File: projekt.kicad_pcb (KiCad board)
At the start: 2 copper layers, 75 x 35 mm, 32 parts, among them J1 Conn_Coaxial, J2 OLED, SW1 SW_DIP_x01, U1 AD8307, U2 L7805

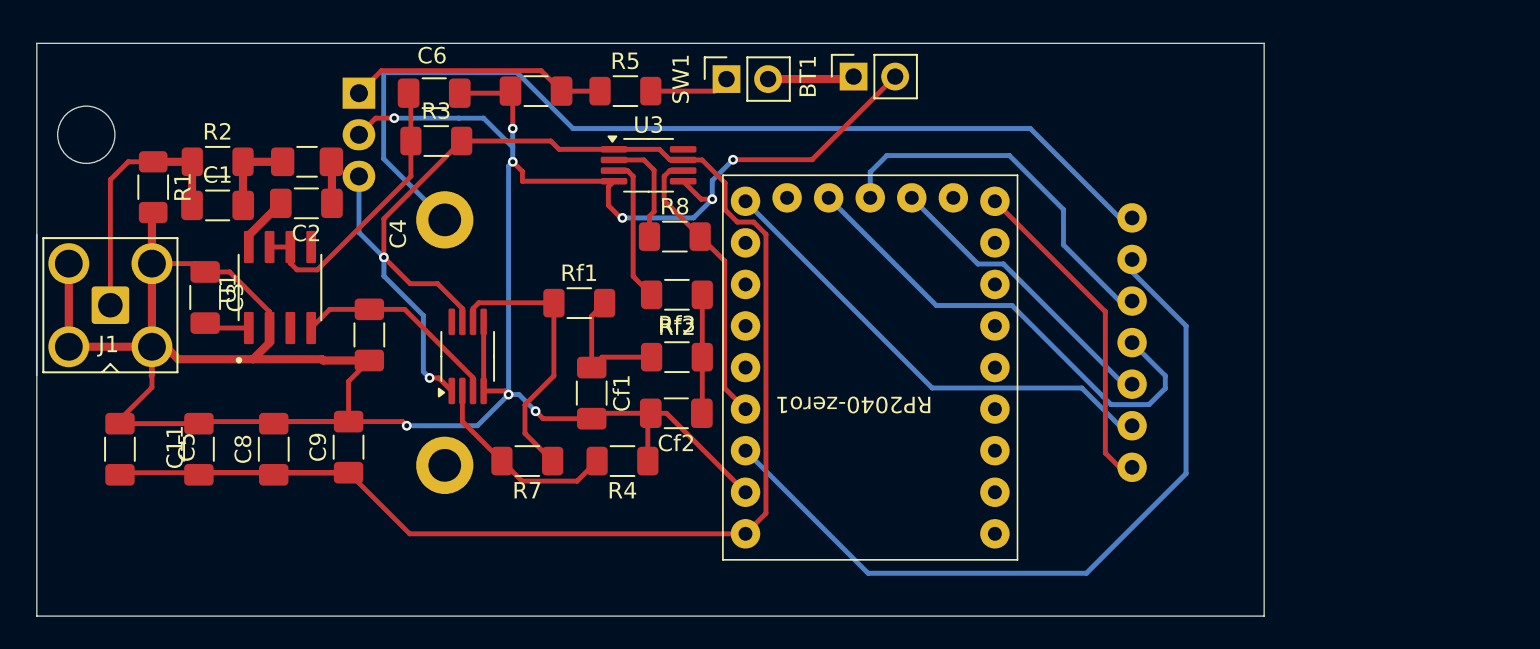
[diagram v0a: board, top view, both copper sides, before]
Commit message: dodane C10
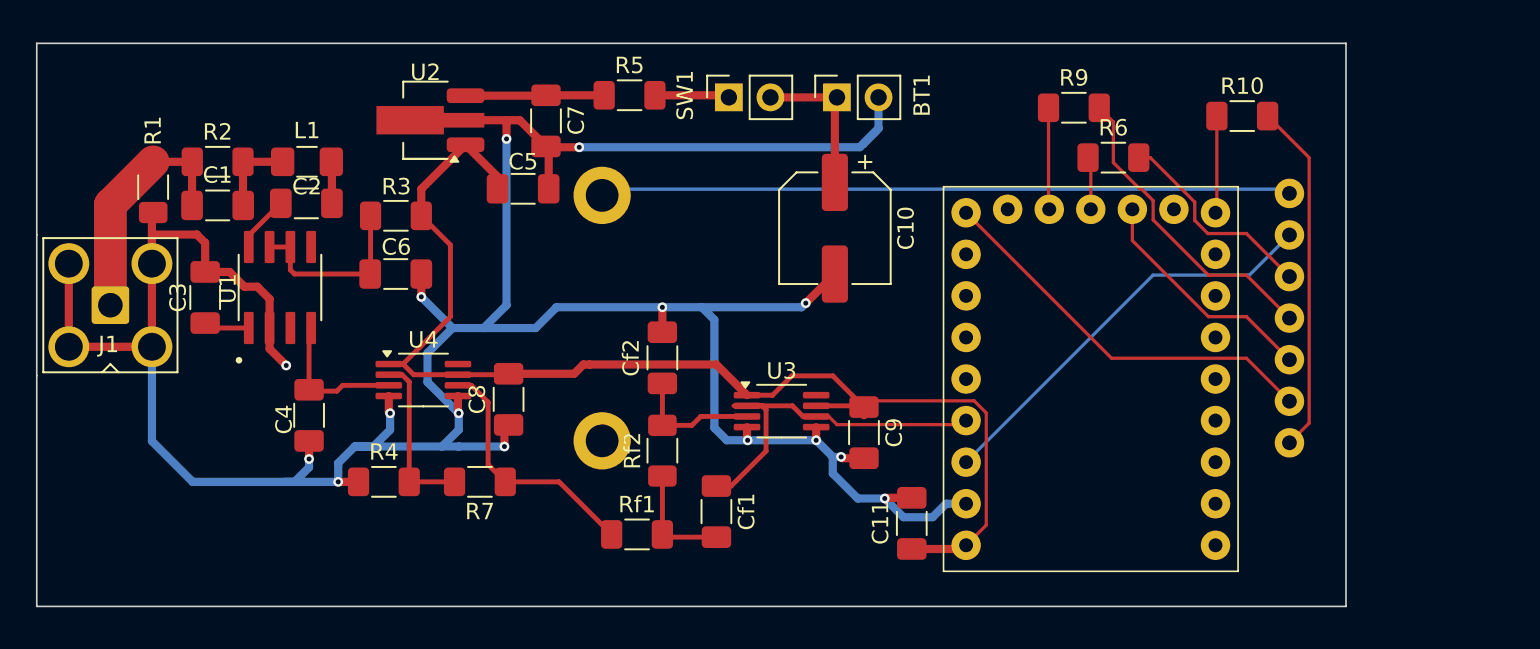
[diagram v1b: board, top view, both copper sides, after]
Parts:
- removed R8: 1k, Resistor_SMD:R_1206_3216Metric_Pad1.30x1.75mm_HandSolder
- removed Rf3: 10k, Resistor_SMD:R_1206_3216Metric_Pad1.30x1.75mm_HandSolder
- added C10: 10u, Capacitor_SMD:CP_Elec_6.3x5.3, F.Cu at (61.5, 33.4)
- added R10: 10, Resistor_SMD:R_1206_3216Metric_Pad1.30x1.75mm_HandSolder, F.Cu at (86.4, 26.5)
- added R6: 10, Resistor_SMD:R_1206_3216Metric_Pad1.30x1.75mm_HandSolder, F.Cu at (78.5, 29.1)
- added R9: 10, Resistor_SMD:R_1206_3216Metric_Pad1.30x1.75mm_HandSolder, F.Cu at (76.1, 26.0)
- U2: footprint Package_TO_SOT_THT:TO-220-3_Horizontal_TabDown -> Package_TO_SOT_SMD:SOT-89-3_Handsoldering; moved to F.Cu
- moved C11 48.6 mm to (66.2, 51.4)
- moved C9 31.5 mm to (63.2, 45.9), turned to -90 degrees
- moved C5 25.4 mm to (42.4, 31.0), turned to 0 degrees
- moved U3 17.1 mm to (58.2, 44.6)
- moved C8 14.7 mm to (41.5, 43.9), turned to -90 degrees
- moved R4 14.6 mm to (33.9, 48.9), turned to 0 degrees
- moved Rf1 14.6 mm to (49.4, 52.1)
- moved RP2040-zero1 13.5 mm to (86.1, 30.9)
- moved C6 11.3 mm to (34.6, 36.2)
- moved Cf1 10.5 mm to (54.2, 50.7)
- moved J2 9.73 mm to (90.7, 48.9)
- moved C4 6.14 mm to (29.3, 44.8)
- moved Rf2 5.78 mm to (50.9, 47.0), turned to 90 degrees
- moved R3 5.19 mm to (34.6, 32.6)
- moved U2 4.39 mm to (36.4, 26.8), turned to 180 degrees
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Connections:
- Cf1 pad 1: Net-(Cf1-Pad1) -> /RF/RF_OUT
- Cf1 pad 2: GNDPWR -> Net-(Cf1-Pad2)
- Cf2 pad 1: Net-(Cf2-Pad1) -> Net-(U3-+)
- RP2040-zero1 pad 10: /uC/CS -> Net-(RP2040-zero1-GP13)
- RP2040-zero1 pad 12: /uC/SDA -> Net-(RP2040-zero1-GP11)
- RP2040-zero1 pad 13: /uC/SCK -> Net-(RP2040-zero1-GP10)
- Rf1 pad 2: Net-(Cf1-Pad1) -> Net-(Cf1-Pad2)
- Rf2 pad 1: Net-(Cf1-Pad1) -> Net-(Cf1-Pad2)
- Rf2 pad 2: Net-(Cf2-Pad1) -> Net-(U3-+)
- U2 pad 1: Net-(U2-IN) -> VCC
- U2 pad 3: VCC -> Net-(U2-IN)
- U3 pad 2: Net-(U3--) -> /RF/RF_OUT
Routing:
- net VCC: track 126.5 -> 75.0 mm, vias 2 -> 0
- net /uC/3V3: track 46.8 -> 25.5 mm
- net /uC/GND: track 59.7 -> 42.3 mm
- net GNDPWR: track 178.7 -> 194.9 mm, vias 9 -> 15
- net /uC/SDA: track 29.9 -> 19.1 mm
- net /uC/SCK: track 22.7 -> 12.9 mm
- net Net-(Cf1-Pad1): track 8.18 -> 0.00 mm
- net Net-(Cf2-Pad1): track 7.50 -> 0.00 mm
- net Net-(U2-IN): track 15.9 -> 8.52 mm
- net Net-(Cf1-Pad2): track 0.00 -> 7.00 mm
- net Net-(U3--): track 6.88 -> 0.00 mm
- net Net-(RP2040-zero1-GP11): track 0.00 -> 6.22 mm
- net Net-(U1-ENB): track 17.3 -> 11.2 mm
- net Net-(RP2040-zero1-GP13): track 0.00 -> 5.94 mm
- net /RF/RF_OUT: track 17.6 -> 22.5 mm
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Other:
- board size 75 x 35 mm -> 80 x 34.4 mm

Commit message: test111
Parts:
- removed C10: 10u, Capacitor_SMD:CP_Elec_6.3x5.3
- added C12: 100n, Capacitor_SMD:C_1206_3216Metric_Pad1.33x1.80mm_HandSolder, F.Cu at (66.3, 51.5)
- C11: value 100n -> 10u; footprint Capacitor_SMD:C_1206_3216Metric_Pad1.33x1.80mm_HandSolder -> Capacitor_SMD:CP_Elec_6.3x5.3
- moved C11 16.8 mm to (63.8, 34.8)
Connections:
- C11 pad 1: GNDPWR -> VCC
- C11 pad 2: VCC -> GNDPWR
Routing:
- net GNDPWR: track 194.9 -> 192.2 mm, vias 15 -> 14

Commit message: test2
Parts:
- added C10: 10n, Capacitor_SMD:C_1206_3216Metric_Pad1.33x1.80mm_HandSolder, F.Cu at (99.8, 25.1)
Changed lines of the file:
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@@
+	)
+	(footprint "Capacitor_SMD:C_1206_3216Metric_Pad1.33x1.80mm_HandSolder"
+		(layer "F.Cu")
+		(at 99.7835 25.146)
+		(descr "Capacitor SMD 1206 (3216 Metric), square (rectangular) end terminal, IPC_7351 nominal with elongated pad for handsoldering. (Body size source: IPC-SM-782 page 76, https://www.pcb-3d.com/wordpress/wp-content/uploads/ipc-sm-782a_amendment_1_and_2.pdf), generated with kicad-footprint-generator")
+		(tags "capacitor handsolder")
+		(property "Reference" "C10"
+			(at 0 -1.85 0)
+			(layer "F.SilkS")
+			(effects
+				(font
+					(size 1 1)
+					(thickness 0.15)
+				)
+			)
+		)
+		(property "Value" "10n"
+			(at 0 1.85 0)
+			(layer "F.Fab")
+			(effects
+				(font
+					(size 1 1)
+					(thickness 0.15)
+				)
+			)
+		)
+		(property "Footprint" "Capacitor_SMD:C_1206_3216Metric_Pad1.33x1.80mm_HandSolder"
+			(at 0 0 0)
+			(unlocked yes)
+			(layer "F.Fab")
+			(hide yes)
+			(effects
+				(font
+					(size 1.27 1.27)
+					(thickness 0.15)
+				)
+			)
+		)
+		(property "Datasheet" ""
+			(at 0 0 0)
+			(unlocked yes)
+			(layer "F.Fab")
+			(hide yes)
+			(effects
+				(font
+					(size 1.27 1.27)
+					(thickness 0.15)
+				)
+			)
+		)
+		(property "Description" "Unpolarized capacitor"
+			(at 0 0 0)
+			(unlocked yes)
+			(layer "F.Fab")
+			(hide yes)
+			(effects
+				(font
+					(size 1.27 1.27)
+					(thickness 0.15)
+				)
+			)
+		)
+		(property ki_fp_filters "C_*")
+		(sheetname "uC")
+		(sheetfile "uC.kicad_sch")
+		(attr smd)
+		(fp_line
+			(start -0.711252 -0.91)
+			(end 0.711252 -0.91)
+			(stroke
+				(width 0.12)
+				(type solid)
+			)
+			(layer "F.SilkS")
+		)
+		(fp_line
+			(start -0.711252 0.91)
+			(end 0.711252 0.91)
+			(stroke
+				(width 0.12)
+				(type solid)
+			)
+			(layer "F.SilkS")
+		)
+		(fp_line
+			(start -2.48 -1.15)
+			(end 2.48 -1.15)
+			(stroke
+				(width 0.05)
+				(type solid)
+			)
+			(layer "F.CrtYd")
+		)
+		(fp_line
+			(start -2.48 1.15)
+			(end -2.48 -1.15)
+			(stroke
+				(width 0.05)
+				(type solid)
+			)
+			(layer "F.CrtYd")
+		)
+		(fp_line
+			(start 2.48 -1.15)
+			(end 2.48 1.15)
+			(stroke
+				(width 0.05)
+				(type solid)
+			)
+			(layer "F.CrtYd")
+		)
+		(fp_line
+			(start 2.48 1.15)
+			(end -2.48 1.15)
+			(stroke
+				(width 0.05)
+				(type solid)
+			)
+			(layer "F.CrtYd")
+		)
+		(fp_line
+			(start -1.6 -0.8)
+			(end 1.6 -0.8)
+			(stroke
+				(width 0.1)
+				(type solid)
+			)
+			(layer "F.Fab")
+		)
+		(fp_line
+			(start -1.6 0.8)
+			(end -1.6 -0.8)
+			(stroke
+				(width 0.1)
+				(type solid)
+			)
+			(layer "F.Fab")
+		)
+		(fp_line
+			(start 1.6 -0.8)
+			(end 1.6 0.8)
+			(stroke
+				(width 0.1)
+				(type solid)
+			)
+			(layer "F.Fab")
+		)
+		(fp_line
+			(start 1.6 0.8)
+			(end -1.6 0.8)
+			(stroke
+				(width 0.1)
+				(type solid)
+			)
+			(layer "F.Fab")
+		)
+		(fp_text user "${REFERENCE}"
+			(at 0 0 0)
+			(layer "F.Fab")
+			(effects
+				(font
+					(size 0.8 0.8)
+					(thickness 0.12)
+				)
+			)
+		)
+		(pad "1" smd roundrect
+			(at -1.5625 0)
+			(size 1.325 1.8)
+			(layers "F.Cu" "F.Paste" "F.Mask")
+			(roundrect_rratio 0.188679)
+			(net 5 "VCC")
+			(pintype "passive")
+		)
+		(pad "2" smd roundrect
+			(at 1.5625 0)
+			(size 1.325 1.8)
+			(layers "F.Cu" "F.Paste" "F.Mask")
+			(roundrect_rratio 0.188679)
+			(net 1 "GNDPWR")
+			(pintype "passive")
+		)
+		(model "${KICAD8_3DMODEL_DIR}/Capacitor_SMD.3dshapes/C_1206_3216Metric.wrl"
+			(offset
+				(xyz 0 0 0)
+			)
+			(scale
+				(xyz 1 1 1)
+			)
+			(rotate
+				(xyz 0 0 0)
+			)
+		)
 	)
 	(footprint "Capacitor_SMD:C_1206_3216Metric_Pad1.33x1.80mm_HandSolder"

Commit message: Kondensator usunięty Test2
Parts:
- removed C10: 10n, Capacitor_SMD:C_1206_3216Metric_Pad1.33x1.80mm_HandSolder
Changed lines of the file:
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@@
-	)
-	(footprint "Capacitor_SMD:C_1206_3216Metric_Pad1.33x1.80mm_HandSolder"
-		(layer "F.Cu")
-		(at 99.7835 25.146)
-		(descr "Capacitor SMD 1206 (3216 Metric), square (rectangular) end terminal, IPC_7351 nominal with elongated pad for handsoldering. (Body size source: IPC-SM-782 page 76, https://www.pcb-3d.com/wordpress/wp-content/uploads/ipc-sm-782a_amendment_1_and_2.pdf), generated with kicad-footprint-generator")
-		(tags "capacitor handsolder")
-		(property "Reference" "C10"
-			(at 0 -1.85 0)
-			(layer "F.SilkS")
-			(effects
-				(font
-					(size 1 1)
-					(thickness 0.15)
-				)
-			)
-		)
-		(property "Value" "10n"
-			(at 0 1.85 0)
-			(layer "F.Fab")
-			(effects
-				(font
-					(size 1 1)
-					(thickness 0.15)
-				)
-			)
-		)
-		(property "Footprint" "Capacitor_SMD:C_1206_3216Metric_Pad1.33x1.80mm_HandSolder"
-			(at 0 0 0)
-			(unlocked yes)
-			(layer "F.Fab")
-			(hide yes)
-			(effects
-				(font
-					(size 1.27 1.27)
-					(thickness 0.15)
-				)
-			)
-		)
-		(property "Datasheet" ""
-			(at 0 0 0)
-			(unlocked yes)
-			(layer "F.Fab")
-			(hide yes)
-			(effects
-				(font
-					(size 1.27 1.27)
-					(thickness 0.15)
-				)
-			)
-		)
-		(property "Description" "Unpolarized capacitor"
-			(at 0 0 0)
-			(unlocked yes)
-			(layer "F.Fab")
-			(hide yes)
-			(effects
-				(font
-					(size 1.27 1.27)
-					(thickness 0.15)
-				)
-			)
-		)
-		(property ki_fp_filters "C_*")
-		(sheetname "uC")
-		(sheetfile "uC.kicad_sch")
-		(attr smd)
-		(fp_line
-			(start -0.711252 -0.91)
-			(end 0.711252 -0.91)
-			(stroke
-				(width 0.12)
-				(type solid)
-			)
-			(layer "F.SilkS")
-		)
-		(fp_line
-			(start -0.711252 0.91)
-			(end 0.711252 0.91)
-			(stroke
-				(width 0.12)
-				(type solid)
-			)
-			(layer "F.SilkS")
-		)
-		(fp_line
-			(start -2.48 -1.15)
-			(end 2.48 -1.15)
-			(stroke
-				(width 0.05)
-				(type solid)
-			)
-			(layer "F.CrtYd")
-		)
-		(fp_line
-			(start -2.48 1.15)
-			(end -2.48 -1.15)
-			(stroke
-				(width 0.05)
-				(type solid)
-			)
-			(layer "F.CrtYd")
-		)
-		(fp_line
-			(start 2.48 -1.15)
-			(end 2.48 1.15)
-			(stroke
-				(width 0.05)
-				(type solid)
-			)
-			(layer "F.CrtYd")
-		)
-		(fp_line
-			(start 2.48 1.15)
-			(end -2.48 1.15)
-			(stroke
-				(width 0.05)
-				(type solid)
-			)
-			(layer "F.CrtYd")
-		)
-		(fp_line
-			(start -1.6 -0.8)
-			(end 1.6 -0.8)
-			(stroke
-				(width 0.1)
-				(type solid)
-			)
-			(layer "F.Fab")
-		)
-		(fp_line
-			(start -1.6 0.8)
-			(end -1.6 -0.8)
-			(stroke
-				(width 0.1)
-				(type solid)
-			)
-			(layer "F.Fab")
-		)
-		(fp_line
-			(start 1.6 -0.8)
-			(end 1.6 0.8)
-			(stroke
-				(width 0.1)
-				(type solid)
-			)
-			(layer "F.Fab")
-		)
-		(fp_line
-			(start 1.6 0.8)
-			(end -1.6 0.8)
-			(stroke
-				(width 0.1)
-				(type solid)
-			)
-			(layer "F.Fab")
-		)
-		(fp_text user "${REFERENCE}"
-			(at 0 0 0)
-			(layer "F.Fab")
-			(effects
-				(font
-					(size 0.8 0.8)
-					(thickness 0.12)
-				)
-			)
-		)
-		(pad "1" smd roundrect
-			(at -1.5625 0)
-			(size 1.325 1.8)
-			(layers "F.Cu" "F.Paste" "F.Mask")
-			(roundrect_rratio 0.188679)
-			(net 5 "VCC")
-			(pintype "passive")
-		)
-		(pad "2" smd roundrect
-			(at 1.5625 0)
-			(size 1.325 1.8)
-			(layers "F.Cu" "F.Paste" "F.Mask")
-			(roundrect_rratio 0.188679)
-			(net 1 "GNDPWR")
-			(pintype "passive")
-		)
-		(model "${KICAD8_3DMODEL_DIR}/Capacitor_SMD.3dshapes/C_1206_3216Metric.wrl"
-			(offset
-				(xyz 0 0 0)
-			)
-			(scale
-				(xyz 1 1 1)
-			)
-			(rotate
-				(xyz 0 0 0)
-			)
-		)
 	)
 	(footprint "Capacitor_SMD:C_1206_3216Metric_Pad1.33x1.80mm_HandSolder"

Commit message: poprawione ścieżki
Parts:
- moved C11 16.3 mm to (47.6, 37.0), turned to 0 degrees
- moved R1 7.65 mm to (23.0, 37.8), turned to 90 degrees
- moved C1 5.90 mm to (27.0, 37.0)
- moved C3 5.90 mm to (26.2, 42.6)
- moved U1 5.90 mm to (30.8, 42.0)
- moved C2 5.90 mm to (32.4, 36.8)
- moved L1 5.90 mm to (32.4, 34.3)
- moved R2 5.90 mm to (27.0, 34.3)
- moved C4 5.77 mm to (34.9, 46.3)
- moved BT1 5.21 mm to (66.8, 25.4)
- moved C12 5.21 mm to (71.5, 51.5)
- moved R9 5.21 mm to (81.3, 26.0)
- moved RP2040-zero1 5.21 mm to (91.3, 30.9)
- moved C5 5.21 mm to (47.6, 31.0)
- moved C6 5.21 mm to (39.8, 36.2)
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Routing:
- net V_BAT: track 9.31 -> 4.24 mm
- net Net-(U1-ENB): track 11.2 -> 15.8 mm
- net VCC: track 75.0 -> 78.7 mm
- net Net-(J1-In): track 14.9 -> 13.5 mm
- net /RF/A: track 10.2 -> 8.89 mm
- net /RF/RF_OUT: track 22.5 -> 21.2 mm
- net Net-(R7-Pad1): track 15.4 -> 16.0 mm
- net GNDPWR: track 192.2 -> 192.4 mm, vias 14 -> 16
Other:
- board size 80 x 34.4 mm -> 85.1 x 34.4 mm

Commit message: ostatnie zmiany 09.08.2024
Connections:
- J2 pad 1: /uC/GND -> GNDPWR
- J2 pad 8: /uC/GND -> GNDPWR
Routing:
- net /uC/GND: track 42.3 -> 0.00 mm
- net GNDPWR: track 192.4 -> 193.7 mm
- added copper zone on B.Cu, net GNDPWR

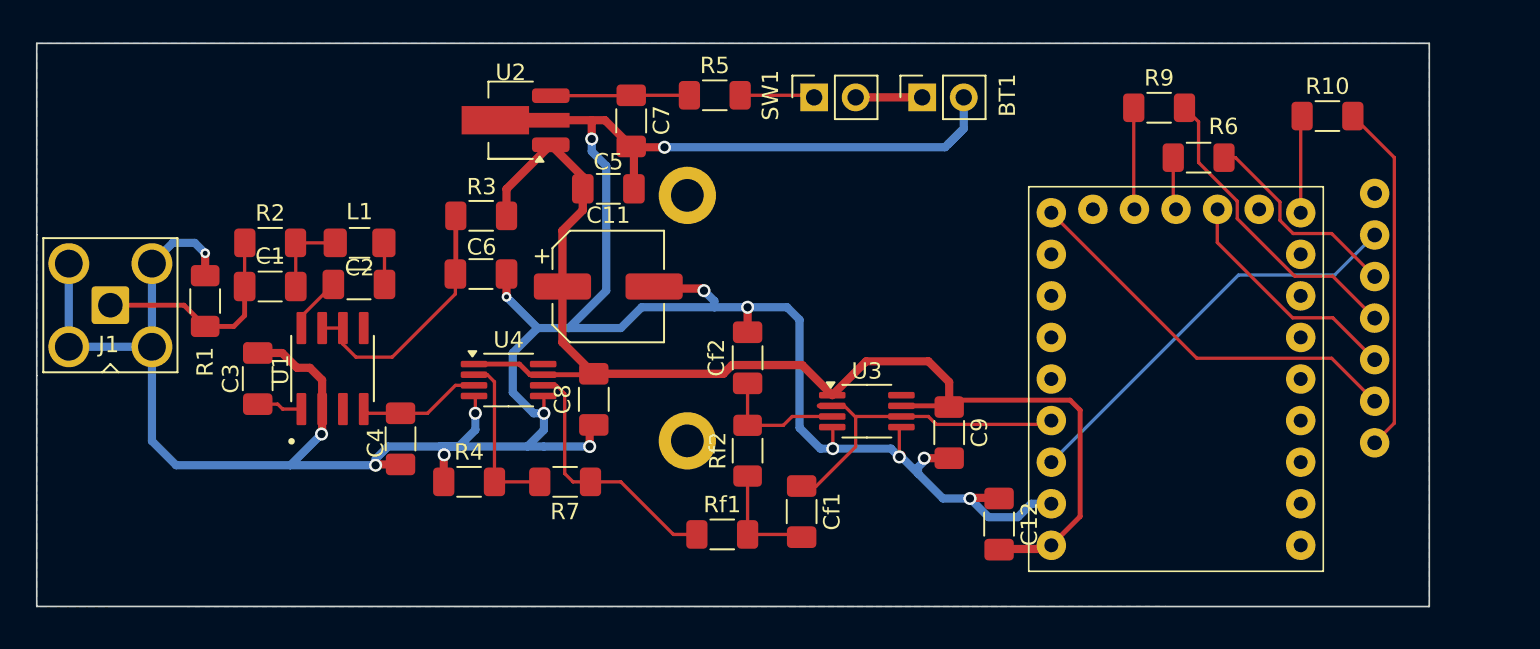
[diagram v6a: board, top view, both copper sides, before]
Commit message: usunięte część ostrzeżeń i błędów
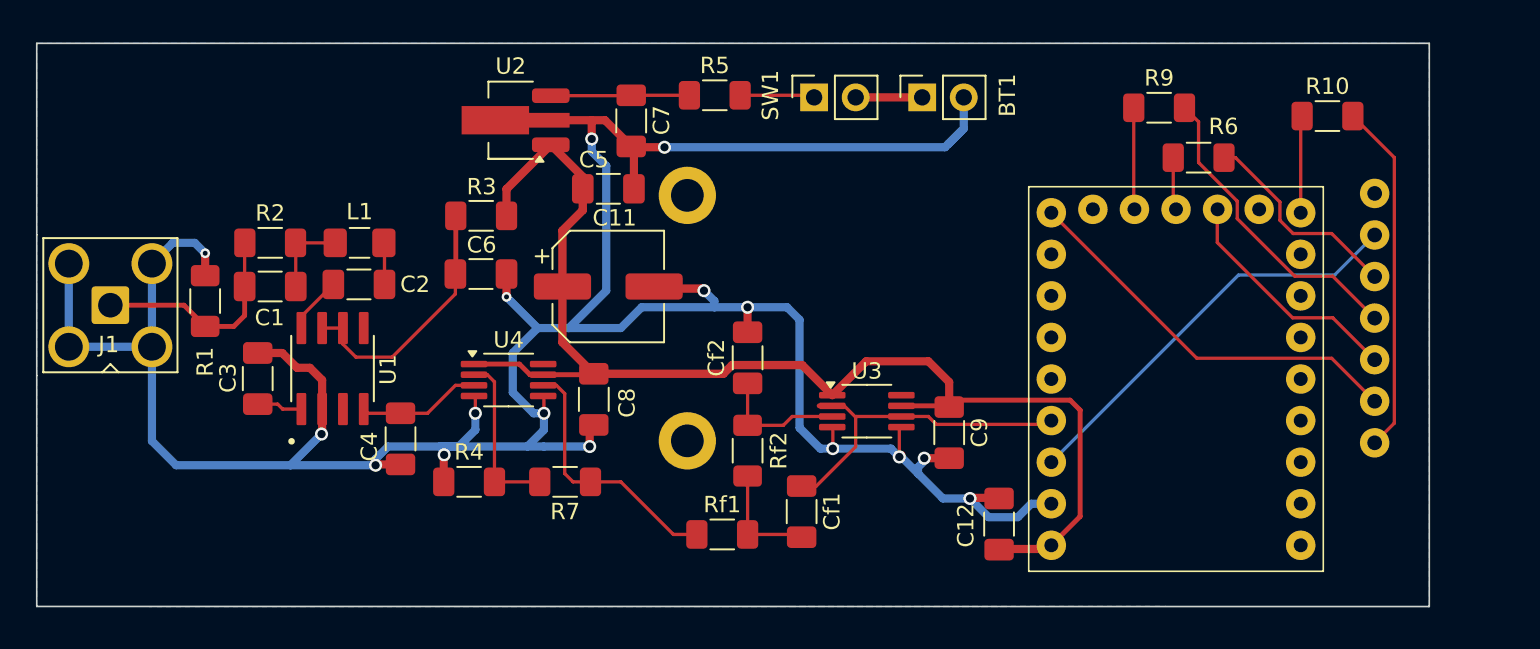
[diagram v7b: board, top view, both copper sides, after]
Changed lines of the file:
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@@
 		(at 30.7705 41.972 90)
 		(property "Reference" "U1"
-			(at -0.065 -3.175 90)
+			(at -0.065 3.3925 90)
 			(layer "F.SilkS")
 			(effects
@@
 		(tags "capacitor handsolder")
 		(property "Reference" "C8"
-			(at 0 1.905 90)
+			(at 0.2155 -2.032 90)
 			(layer "F.SilkS")
 			(effects
@@
 		(tags "capacitor handsolder")
 		(property "Reference" "C6"
-			(at 0.0385 -1.651 0)
+			(at 0.0385 -1.778 0)
 			(layer "F.SilkS")
 			(effects
@@
 		(tags "SOT-89-3 Handsoldering")
 		(property "Reference" "U2"
-			(at 0 2.921 0)
+			(at 0 3.302 0)
 			(layer "F.SilkS")
 			(effects
@@
 		(tags "capacitor handsolder")
 		(property "Reference" "C3"
-			(at 0 1.651 90)
+			(at -0.0385 1.8145 90)
 			(layer "F.SilkS")
 			(effects
@@
 		(tags "capacitor handsolder")
 		(property "Reference" "C5"
-			(at 0 -1.651 0)
+			(at -0.889 -1.778 0)
 			(layer "F.SilkS")
 			(effects
@@
 		(tags "capacitor handsolder")
 		(property "Reference" "C1"
-			(at 0 -1.85 0)
+			(at -0.0365 1.905 0)
 			(layer "F.SilkS")
 			(effects
@@
 		(tags "resistor handsolder")
 		(property "Reference" "Rf2"
-			(at 0 -1.82 90)
+			(at 0 1.905 90)
 			(layer "F.SilkS")
 			(effects
@@
 		(tags "capacitor handsolder")
 		(property "Reference" "C12"
-			(at 0 -1.85 90)
+			(at 0.0885 2.032 90)
 			(layer "F.SilkS")
 			(effects
@@
 		(tags "capacitor handsolder")
 		(property "Reference" "C4"
-			(at 0.254 1.524 90)
+			(at 0.4695 1.905 90)
 			(layer "F.SilkS")
 			(effects
@@
 		(tags "capacitor electrolytic")
 		(property "Reference" "C11"
-			(at 0 -4.35 0)
+			(at 0.387 -4.191 0)
 			(layer "F.SilkS")
 			(effects
@@
 		(tags "capacitor handsolder")
 		(property "Reference" "C2"
-			(at -0.0385 1.016 0)
+			(at -3.431 0 0)
 			(layer "F.SilkS")
 			(effects
@@
 		(min_thickness 0.25)
 		(filled_areas_thickness no)
-		(fill
+		(fill yes
 			(thermal_gap 0.5)
 			(thermal_bridge_width 0.5)

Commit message: ostateczna wersja do produkcji
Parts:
- added REF**: MountingHole_2.5mm_Pad_TopBottom, MountingHole:MountingHole_2.5mm_Pad_TopBottom, F.Cu at (99.0, 53.0)
- added REF**: MountingHole_2.5mm_Pad_TopBottom, MountingHole:MountingHole_2.5mm_Pad_TopBottom, F.Cu at (99.0, 25.0)
- added REF**: MountingHole_2.5mm_Pad_TopBottom, MountingHole:MountingHole_2.5mm_Pad_TopBottom, F.Cu at (16.0, 53.0)
- added REF**: MountingHole_2.5mm_Pad_TopBottom, MountingHole:MountingHole_2.5mm_Pad_TopBottom, F.Cu at (16.0, 25.0)
- moved J1 0.20 mm to (17.0, 38.1)
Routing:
- net GNDPWR: track 193.7 -> 223.5 mm
- net /uC/3V3: track 25.5 -> 52.1 mm, vias 0 -> 2
- net /uC/RST: track 14.6 -> 16.4 mm
- net /uC/SDA: track 19.0 -> 19.8 mm
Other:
- board size 85.1 x 34.4 mm -> 90 x 35 mm
